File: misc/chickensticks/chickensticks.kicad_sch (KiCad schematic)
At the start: 4 parts

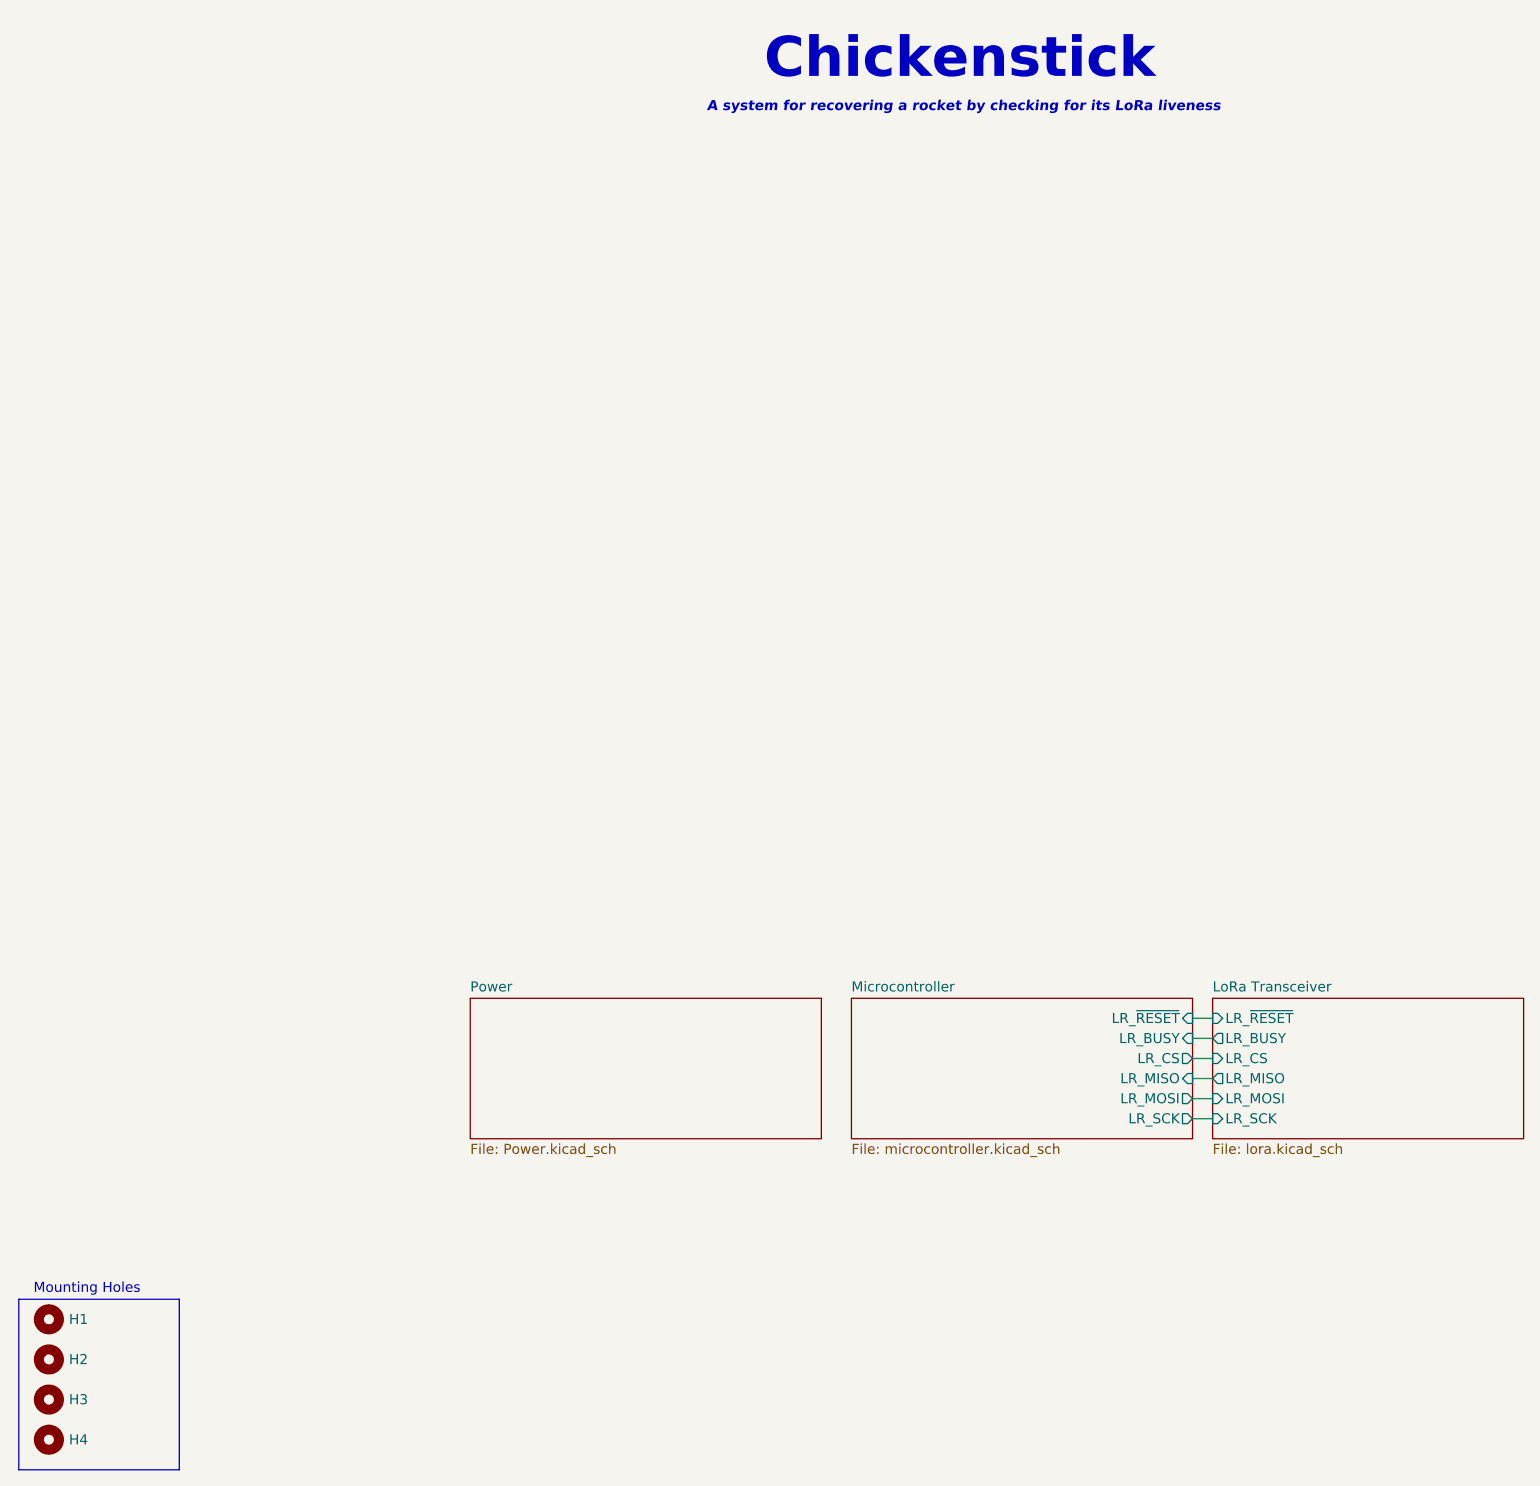
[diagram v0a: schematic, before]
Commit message: Simplify chickensticks, get isospi-tx ready, and update some cubemx projects
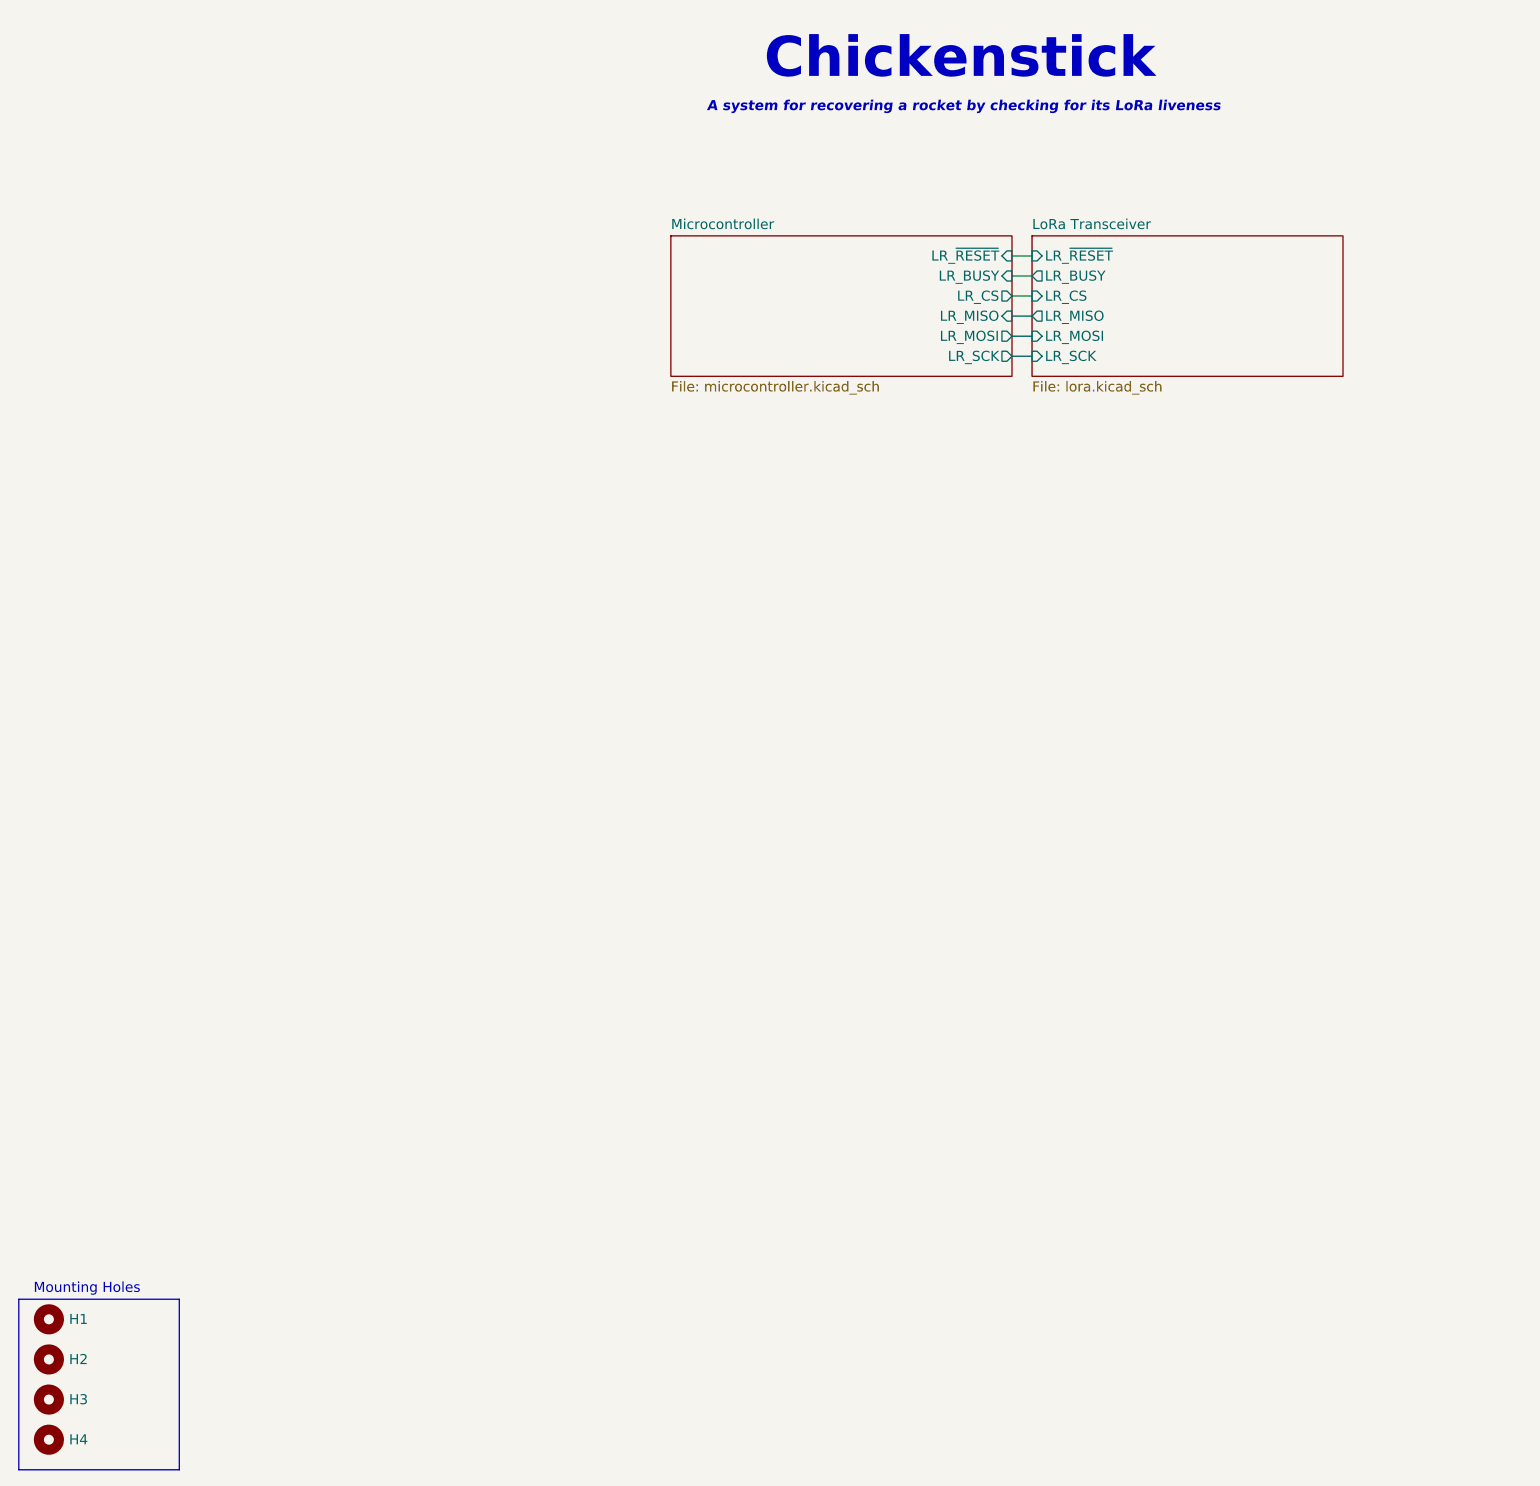
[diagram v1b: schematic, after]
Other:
- removed sheet Power
- company: Aggie Propulsion & Rocketry Lab -> (none)
- title: Chickenstick -> (none)
